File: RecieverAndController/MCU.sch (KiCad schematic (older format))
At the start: 11 parts

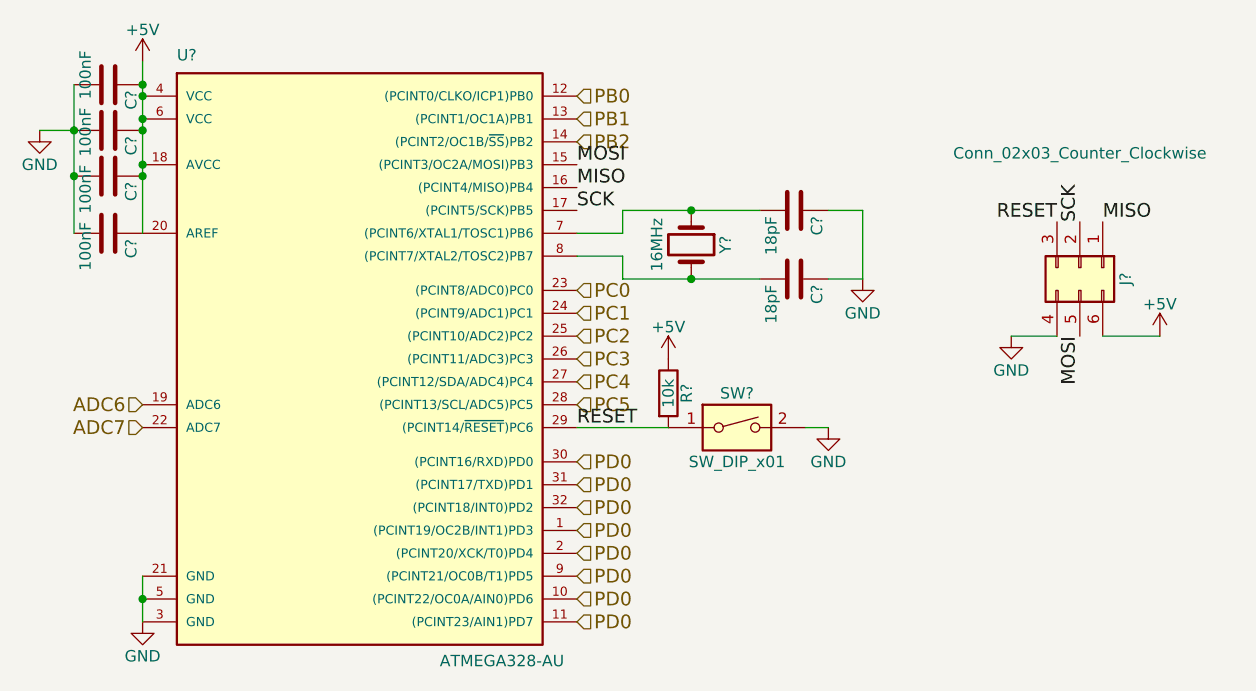
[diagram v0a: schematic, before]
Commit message: adding footprints to schematic
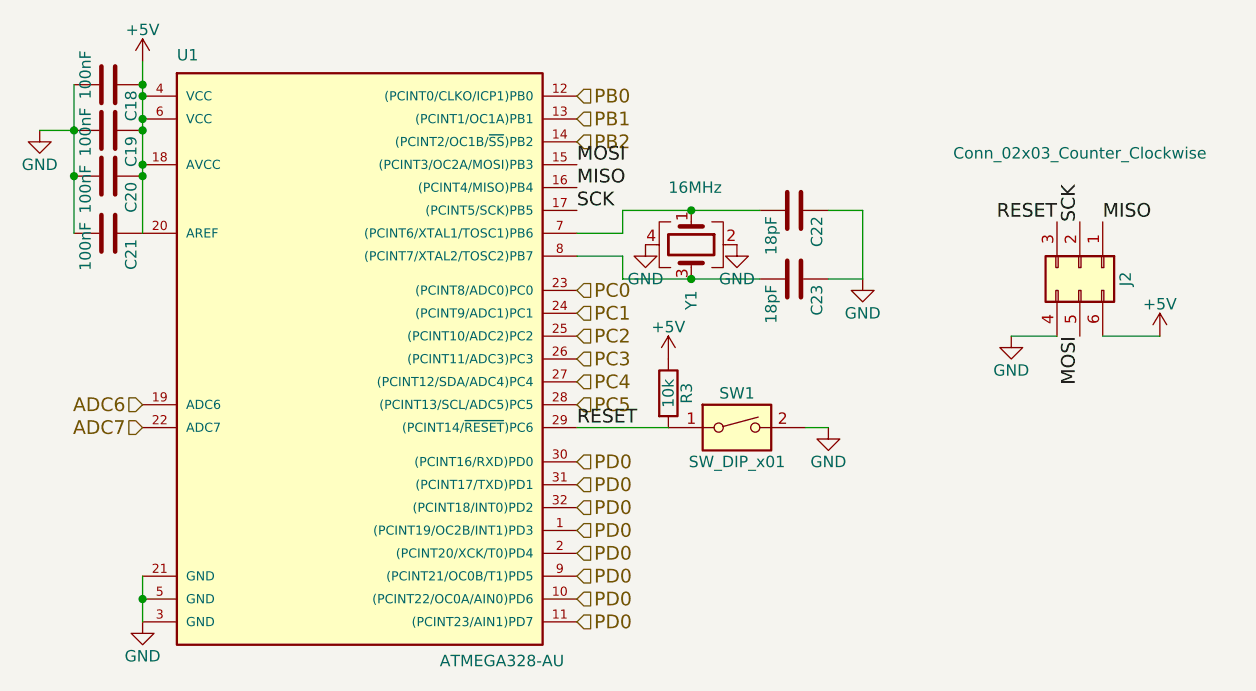
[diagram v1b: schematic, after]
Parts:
- removed Y?: 16MHz, symbol Crystal
- added Y1: 16MHz, Custom:SER3686DKR-ND, symbol Crystal_GND24
- C18, C19, C20, C21, C22, C23: renamed from C?; footprint (none) -> Capacitors_SMD:C_0603
- J2: renamed from J?; footprint (none) -> Pin_Headers:Pin_Header_Angled_2x03_Pitch2.54mm
- R3: renamed from R?; footprint (none) -> Resistors_SMD:R_0603
- SW1: renamed from SW?; footprint (none) -> Custom:CKN10291CT-ND
- gave numbers to parts that had none: 1
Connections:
- net GND: now also Y1.2, Y1.4
- net at C22.2, U1.7 ((PCINT6/XTAL1/TOSC1)PB6): now also Y1.1
- net at C23.2, U1.8 ((PCINT7/XTAL2/TOSC2)PB7): now also Y1.3
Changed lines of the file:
@@
 $EndDescr
 $Comp
-L ATMEGA328-AU U?
+L ATMEGA328-AU U1
 U 1 1 5A997AB6
 P 2850 2400
-F 0 "U?" H 2100 3650 50  0000 L BNN
+F 0 "U1" H 2100 3650 50  0000 L BNN
 F 1 "ATMEGA328-AU" H 3250 1000 50  0000 L BNN
 F 2 "Housings_QFP:TQFP-32_7x7mm_Pitch0.8mm" H 2850 2400 50  0001 C CIN
@@
 $EndComp
 $Comp
-L C C?
+L C C19
 U 1 1 5A998588
 P 1800 1450
-F 0 "C?" H 1825 1550 50  0000 L CNN
+F 0 "C19" H 1825 1550 50  0000 L CNN
 F 1 "100nF" H 1700 1350 50  0000 L CNN
-F 2 "" H 1838 1300 50  0001 C CNN
+F 2 "Capacitors_SMD:C_0603" H 1838 1300 50  0001 C CNN
 F 3 "" H 1800 1450 50  0001 C CNN
 	1    1800 1450
@@
 $EndComp
 $Comp
-L C C?
+L C C18
 U 1 1 5A998772
 P 1800 1250
-F 0 "C?" H 1825 1350 50  0000 L CNN
+F 0 "C18" H 1825 1350 50  0000 L CNN
 F 1 "100nF" H 1650 1150 50  0000 L CNN
-F 2 "" H 1838 1100 50  0001 C CNN
+F 2 "Capacitors_SMD:C_0603" H 1838 1100 50  0001 C CNN
 F 3 "" H 1800 1250 50  0001 C CNN
 	1    1800 1250
@@
 Connection ~ 1950 1250
 $Comp
-L GND #PWR?
+L GND #PWR03
 U 1 1 5A9988A7
 P 1500 1450
-F 0 "#PWR?" H 1500 1200 50  0001 C CNN
+F 0 "#PWR03" H 1500 1200 50  0001 C CNN
 F 1 "GND" H 1500 1300 50  0000 C CNN
 F 2 "" H 1500 1450 50  0001 C CNN
@@
 	1650 1250 1650 1900
 $Comp
-L C C?
+L C C20
 U 1 1 5A998944
 P 1800 1650
-F 0 "C?" H 1825 1750 50  0000 L CNN
+F 0 "C20" H 1825 1750 50  0000 L CNN
 F 1 "100nF" H 1750 1550 50  0000 L CNN
-F 2 "" H 1838 1500 50  0001 C CNN
+F 2 "Capacitors_SMD:C_0603" H 1838 1500 50  0001 C CNN
 F 3 "" H 1800 1650 50  0001 C CNN
 	1    1800 1650
@@
 Connection ~ 1650 1450
 $Comp
-L C C?
+L C C21
 U 1 1 5A998F30
 P 1800 1900
-F 0 "C?" H 1825 2000 50  0000 L CNN
+F 0 "C21" H 1825 2000 50  0000 L CNN
 F 1 "100nF" H 1750 1800 50  0000 L CNN
-F 2 "" H 1838 1750 50  0001 C CNN
+F 2 "Capacitors_SMD:C_0603" H 1838 1750 50  0001 C CNN
 F 3 "" H 1800 1900 50  0001 C CNN
 	1    1800 1900
@@
 Connection ~ 1650 1650
 $Comp
-L GND #PWR?
+L GND #PWR04
 U 1 1 5A99900B
 P 1950 3600
-F 0 "#PWR?" H 1950 3350 50  0001 C CNN
+F 0 "#PWR04" H 1950 3350 50  0001 C CNN
 F 1 "GND" H 1950 3450 50  0000 C CNN
 F 2 "" H 1950 3600 50  0001 C CNN
@@
 Connection ~ 1950 3500
 $Comp
-L Crystal Y?
-U 1 1 5A999A2A
-P 4350 1950
-F 0 "Y?" H 4350 2100 50  0000 C CNN
-F 1 "16MHz" H 4350 1800 50  0000 C CNN
-F 2 "" H 4350 1950 50  0001 C CNN
-F 3 "" H 4350 1950 50  0001 C CNN
-	1    4350 1950
-	0    1    1    0
-$EndComp
-$Comp
-L C C?
+L C C22
 U 1 1 5A999B07
 P 4800 1800
-F 0 "C?" H 4825 1900 50  0000 L CNN
+F 0 "C22" H 4825 1900 50  0000 L CNN
 F 1 "18pF" H 4825 1700 50  0000 L CNN
-F 2 "" H 4838 1650 50  0001 C CNN
+F 2 "Capacitors_SMD:C_0603" H 4838 1650 50  0001 C CNN
 F 3 "" H 4800 1800 50  0001 C CNN
 	1    4800 1800
@@
 $EndComp
 $Comp
-L C C?
+L C C23
 U 1 1 5A999B39
 P 4800 2100
-F 0 "C?" H 4825 2200 50  0000 L CNN
+F 0 "C23" H 4825 2200 50  0000 L CNN
 F 1 "18pF" H 4825 2000 50  0000 L CNN
-F 2 "" H 4838 1950 50  0001 C CNN
+F 2 "Capacitors_SMD:C_0603" H 4838 1950 50  0001 C CNN
 F 3 "" H 4800 2100 50  0001 C CNN
 	1    4800 2100
@@
 Connection ~ 4350 2100
 $Comp
-L GND #PWR?
+L GND #PWR05
 U 1 1 5A999C5D
 P 5100 2100
-F 0 "#PWR?" H 5100 1850 50  0001 C CNN
+F 0 "#PWR05" H 5100 1850 50  0001 C CNN
 F 1 "GND" H 5100 1950 50  0000 C CNN
 F 2 "" H 5100 2100 50  0001 C CNN
@@
 	5100 1800 5100 2100
 $Comp
-L SW_DIP_x01 SW?
+L SW_DIP_x01 SW1
 U 1 1 5A99B501
 P 4550 2750
-F 0 "SW?" H 4550 2900 50  0000 C CNN
+F 0 "SW1" H 4550 2900 50  0000 C CNN
 F 1 "SW_DIP_x01" H 4550 2600 50  0000 C CNN
-F 2 "" H 4550 2750 50  0001 C CNN
+F 2 "Custom:CKN10291CT-ND" H 4550 2750 50  0001 C CNN
 F 3 "" H 4550 2750 50  0001 C CNN
 	1    4550 2750
@@
 $EndComp
 $Comp
-L R R?
+L R R3
 U 1 1 5A99B5A5
 P 4250 2600
-F 0 "R?" V 4330 2600 50  0000 C CNN
+F 0 "R3" V 4330 2600 50  0000 C CNN
 F 1 "10k" V 4250 2600 50  0000 C CNN
-F 2 "" V 4180 2600 50  0001 C CNN
+F 2 "Resistors_SMD:R_0603" V 4180 2600 50  0001 C CNN
 F 3 "" H 4250 2600 50  0001 C CNN
 	1    4250 2600
@@
 	3850 2750 4250 2750
 $Comp
-L GND #PWR?
+L GND #PWR06
 U 1 1 5A99B661
 P 4950 2750
-F 0 "#PWR?" H 4950 2500 50  0001 C CNN
+F 0 "#PWR06" H 4950 2500 50  0001 C CNN
 F 1 "GND" H 4950 2600 50  0000 C CNN
 F 2 "" H 4950 2750 50  0001 C CNN
@@
 	4850 2750 4950 2750
 $Comp
-L Conn_02x03_Counter_Clockwise J?
+L Conn_02x03_Counter_Clockwise J2
 U 1 1 5A99BDD1
 P 6050 2050
-F 0 "J?" H 6100 2250 50  0000 C CNN
+F 0 "J2" H 6100 2250 50  0000 C CNN
 F 1 "Conn_02x03_Counter_Clockwise" V 5550 2050 50  0000 C CNN
-F 2 "" H 6050 2050 50  0001 C CNN
+F 2 "Pin_Headers:Pin_Header_Angled_2x03_Pitch2.54mm" H 6050 2050 50  0001 C CNN
 F 3 "" H 6050 2050 50  0001 C CNN
 	1    6050 2050
@@
 $EndComp
 $Comp
-L GND #PWR?
+L GND #PWR07
 U 1 1 5A99BE0E
 P 5750 2350
-F 0 "#PWR?" H 5750 2100 50  0001 C CNN
+F 0 "#PWR07" H 5750 2100 50  0001 C CNN
 F 1 "GND" H 5750 2200 50  0000 C CNN
 F 2 "" H 5750 2350 50  0001 C CNN
@@
 $EndComp
 $Comp
-L +5V #PWR?
+L +5V #PWR08
 U 1 1 5A99BE38
 P 6400 2350
-F 0 "#PWR?" H 6400 2200 50  0001 C CNN
+F 0 "#PWR08" H 6400 2200 50  0001 C CNN
 F 1 "+5V" H 6400 2490 50  0000 C CNN
 F 2 "" H 6400 2350 50  0001 C CNN
@@
 	6150 2350 6400 2350
 $Comp
-L +5V #PWR?
+L +5V #PWR09
 U 1 1 5A99BEED
 P 1950 1150
-F 0 "#PWR?" H 1950 1000 50  0001 C CNN
+F 0 "#PWR09" H 1950 1000 50  0001 C CNN
 F 1 "+5V" H 1950 1290 50  0000 C CNN
 F 2 "" H 1950 1150 50  0001 C CNN
@@
 $EndComp
 $Comp
-L +5V #PWR?
+L +5V #PWR010
 U 1 1 5A99BF72
 P 4250 2450
-F 0 "#PWR?" H 4250 2300 50  0001 C CNN
+F 0 "#PWR010" H 4250 2300 50  0001 C CNN
 F 1 "+5V" H 4250 2590 50  0000 C CNN
 F 2 "" H 4250 2450 50  0001 C CNN
@@
 Text HLabel 1950 2750 0    60   Input ~ 0
 ADC7
+$Comp
+L Crystal_GND24 Y1
+U 1 1 5AC98DA0
+P 4350 1950
+F 0 "Y1" H 4550 1950 50  0000 L CNN
+F 1 "16MHz" V 4100 1850 50  0000 L CNN
+F 2 "Custom:SER3686DKR-ND" H 4350 1950 50  0001 C CNN
+F 3 "" H 4350 1950 50  0001 C CNN
+	1    4350 1950
+	0    1    1    0
+$EndComp
+$Comp
+L GND #PWR011
+U 1 1 5AC991AC
+P 4150 1950
+F 0 "#PWR011" H 4150 1700 50  0001 C CNN
+F 1 "GND" H 4150 1800 50  0000 C CNN
+F 2 "" H 4150 1950 50  0001 C CNN
+F 3 "" H 4150 1950 50  0001 C CNN
+	1    4150 1950
+	1    0    0    -1
+$EndComp
+$Comp
+L GND #PWR012
+U 1 1 5AC991D6
+P 4550 1950
+F 0 "#PWR012" H 4550 1700 50  0001 C CNN
+F 1 "GND" H 4550 1800 50  0000 C CNN
+F 2 "" H 4550 1950 50  0001 C CNN
+F 3 "" H 4550 1950 50  0001 C CNN
+	1    4550 1950
+	1    0    0    -1
+$EndComp
 $EndSCHEMATC

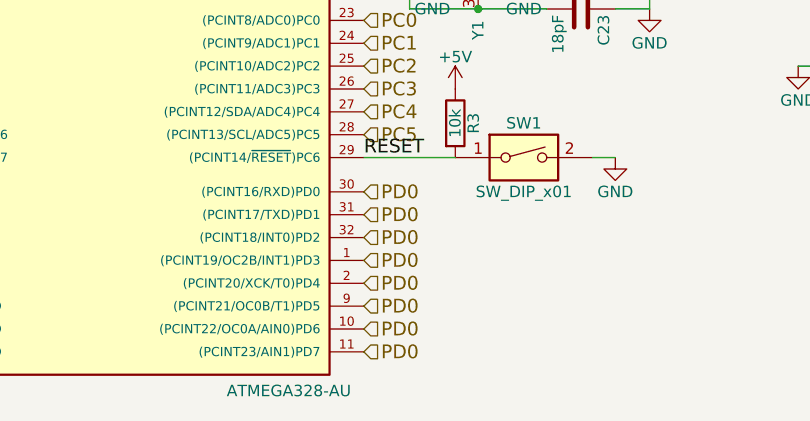
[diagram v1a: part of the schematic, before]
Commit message: adding and fixing reciever
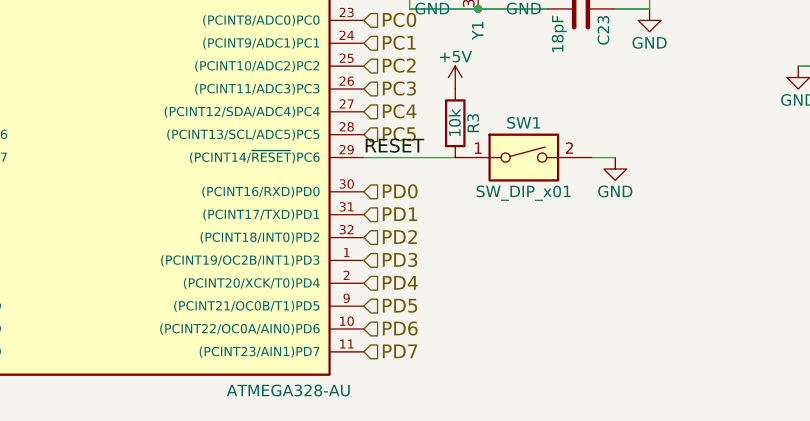
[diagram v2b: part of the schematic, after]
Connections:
- net PD0: no longer U1.1 ((PCINT19/OC2B/INT1)PD3), U1.10 ((PCINT22/OC0A/AIN0)PD6), U1.11 ((PCINT23/AIN1)PD7), U1.2 ((PCINT20/XCK/T0)PD4), U1.31 ((PCINT17/TXD)PD1), U1.32 ((PCINT18/INT0)PD2), U1.9 ((PCINT21/OC0B/T1)PD5)
- new net PD1: U1.31 ((PCINT17/TXD)PD1)
- new net PD2: U1.32 ((PCINT18/INT0)PD2)
- new net PD3: U1.1 ((PCINT19/OC2B/INT1)PD3)
- new net PD4: U1.2 ((PCINT20/XCK/T0)PD4)
- new net PD5: U1.9 ((PCINT21/OC0B/T1)PD5)
- new net PD6: U1.10 ((PCINT22/OC0A/AIN0)PD6)
- new net PD7: U1.11 ((PCINT23/AIN1)PD7)
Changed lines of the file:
@@
 PD0
 Text HLabel 3850 3000 2    60   Input ~ 0
-PD0
+PD1
 Text HLabel 3850 3100 2    60   Input ~ 0
-PD0
+PD2
 Text HLabel 3850 3200 2    60   Input ~ 0
-PD0
+PD3
 Text HLabel 3850 3300 2    60   Input ~ 0
-PD0
+PD4
 Text HLabel 3850 3400 2    60   Input ~ 0
-PD0
+PD5
 Text HLabel 3850 3500 2    60   Input ~ 0
-PD0
+PD6
 Text HLabel 3850 3600 2    60   Input ~ 0
-PD0
+PD7
 Text HLabel 3850 1300 2    60   Input ~ 0
 PB0
